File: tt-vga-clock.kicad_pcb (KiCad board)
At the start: 4 copper layers, 39 x 54 mm, 58 parts, among them J1 USB_C_Receptacle_USB2.0, J2 Conn_01x02, J3 Conn_02x04_Odd_Even, J4 Conn_01x06, J5 613012243121, J6 Conn_02x18_Odd_Even, SW1 B3U-1000P, SW2 B3U-1000P, U1 Caravel_QFN, U2 W25Q32JVSS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

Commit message: pinout for buttons, delete unneeded parts
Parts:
- removed C15: 100nF, Capacitor_SMD:C_0603_1608Metric
- removed C24, C5: 1uF, Capacitor_SMD:C_0603_1608Metric
- removed J4: Conn_01x06, Connector_PinHeader_2.54mm:PinHeader_1x06_P2.54mm_Vertical
- removed J6: Conn_02x18_Odd_Even, Connector_PinHeader_2.54mm:PinHeader_2x18_P2.54mm_Vertical
- removed R11: 5.1k, Resistor_SMD:R_0603_1608Metric
- removed R8: 10k, Resistor_SMD:R_0603_1608Metric
- removed SW2: B3U-1000P, Button_Switch_SMD:SW_SPST_B3U-1000P

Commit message: schematic done
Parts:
- removed J2: Conn_01x02, Connector_JST:JST_PH_B2B-PH-K_1x02_P2.00mm_Vertical
- added C15: 1uF, Capacitor_SMD:C_0603_1608Metric, F.Cu at (135.3, 57.4)
- added C24: 1uF, Capacitor_SMD:C_0603_1608Metric, F.Cu at (135.3, 59.9)
- added C25: 1uF, Capacitor_SMD:C_0603_1608Metric, F.Cu at (135.3, 62.4)
- added C26: 1uF, Capacitor_SMD:C_0603_1608Metric, F.Cu at (135.3, 64.9)
- added C5: 1uF, Capacitor_SMD:C_0603_1608Metric, F.Cu at (135.3, 54.9)
- added NT1: NetTie_2, NetTie:NetTie-2_SMD_Pad0.5mm, F.Cu at (113.9, 80.0)
- added NT2: NetTie_2, NetTie:NetTie-2_SMD_Pad0.5mm, F.Cu at (113.9, 81.5)
- added R11: 5.1k, Resistor_SMD:R_0603_1608Metric, F.Cu at (135.3, 69.9)
- added R16: 10k, Resistor_SMD:R_0603_1608Metric, F.Cu at (139.3, 54.9)
- added R17: 5.1k, Resistor_SMD:R_0603_1608Metric, F.Cu at (139.3, 57.4)
- added R18: 10k, Resistor_SMD:R_0603_1608Metric, F.Cu at (139.3, 59.9)
- added R19: 5.1k, Resistor_SMD:R_0603_1608Metric, F.Cu at (139.3, 62.4)
- added R20: 10k, Resistor_SMD:R_0603_1608Metric, F.Cu at (139.3, 64.9)
- added R21: 5.1k, Resistor_SMD:R_0603_1608Metric, F.Cu at (139.3, 67.4)
- added R22: 500R, Resistor_SMD:R_0603_1608Metric, F.Cu at (139.3, 69.9)
- added R23: 1k, Resistor_SMD:R_0603_1608Metric, F.Cu at (143.3, 54.9)
- added R24: 500R, Resistor_SMD:R_0603_1608Metric, F.Cu at (143.3, 57.4)
- added R25: 1k, Resistor_SMD:R_0603_1608Metric, F.Cu at (143.3, 59.9)
- added R26: 500R, Resistor_SMD:R_0603_1608Metric, F.Cu at (143.3, 62.4)
- added R27: 1k, Resistor_SMD:R_0603_1608Metric, F.Cu at (143.3, 64.9)
- added R8: 10k, Resistor_SMD:R_0603_1608Metric, F.Cu at (135.3, 67.4)
- added SW2: B3U-1000P, Button_Switch_SMD:SW_SPST_B3U-1000P, F.Cu at (148.3, 55.8)
- added SW3: B3U-1000P, Button_Switch_SMD:SW_SPST_B3U-1000P, F.Cu at (148.3, 60.1)
- added SW4: B3U-1000P, Button_Switch_SMD:SW_SPST_B3U-1000P, F.Cu at (148.3, 64.5)
- added SW5: B3U-1000P, Button_Switch_SMD:SW_SPST_B3U-1000P, F.Cu at (148.3, 68.8)
- added TP1: TestPoint, TestPoint:TestPoint_Pad_1.0x1.0mm, F.Cu at (137.3, 78.5)
- added TP2: TestPoint, TestPoint:TestPoint_Pad_1.0x1.0mm, F.Cu at (137.3, 81.5)
- J5: value 613012243121 -> DE15_Receptacle_HighDensity_MountingHoles; footprint TinyTapeout:PinSocket_2x06_P2.54mm_PMODHost1A -> Connector_Dsub:DSUB-15-HD_Female_Horizontal_P2.29x1.98mm_EdgePinOffset8.35mm_Housed_MountingHolesOffset10.89mm
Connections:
- J5 pad 1: /prj_io7 -> /red
- J5 pad 10: /prj_io14 -> GND
- J5 pad 11: GND -> unconnected-(J5-Pad11)
- J5 pad 12: +3V3 -> unconnected-(J5-Pad12)
- J5 pad 2: /prj_io8 -> /green
- J5 pad 3: /prj_io9 -> /blue
- J5 pad 4: /prj_io10 -> unconnected-(J5-Pad4)
- J5 pad 6: +3V3 -> GND
- J5 pad 7: /prj_io11 -> GND
- J5 pad 8: /prj_io12 -> GND
- J5 pad 9: /prj_io13 -> unconnected-(J5-Pad9)
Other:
- board text added: "Matt Venn"
- board text added: "TT3p5 VGA clock"
- board text removed: "(C) 2023 Pat Deegan"
- board text removed: "Caravel MVP Template"
- board text removed: "Sample Layout"
- board text removed: "This is just an example floorplan I created to get things started. Assuming you've changed the schematic, be sure to update with the appropriate Re-link/delete/replace options selected. Have fun!"
- board text removed: "v1.1"

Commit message: start layout
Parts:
- removed C11, C12, C13, C14, C17, C8: 100nF, Capacitor_SMD:C_0603_1608Metric
- removed C16: 10uF, Capacitor_SMD:C_0805_2012Metric
- removed C3: 6800pF, Capacitor_SMD:C_0603_1608Metric
- removed C4: 1uF, Capacitor_SMD:C_0603_1608Metric
- removed R2: 10k, Resistor_SMD:R_0603_1608Metric
- removed R3: 5.1k, Resistor_SMD:R_0603_1608Metric
- removed SW1: B3U-1000P, Button_Switch_SMD:SW_SPST_B3U-1000P
- added NT3: NetTie_2, NetTie:NetTie-2_SMD_Pad0.5mm, F.Cu at (104.9, 56.8)
- added TP3: TestPoint, TestPoint:TestPoint_Pad_1.0x1.0mm, F.Cu at (101.8, 49.0)
- X1: value 10MHz -> 31.5MHz
- moved SW2 60.6 mm to (95.3, 26.3), turned to 180 degrees
- moved R11 55.0 mm to (98.2, 29.3), turned to 180 degrees
- moved R8 54.5 mm to (99.5, 26.3), turned to -90 degrees
- moved FID2 50.4 mm to (127.1, 78.4)
- moved C5 48.1 mm to (94.6, 29.3)
- moved R23 41.1 mm to (103.0, 62.5), turned to -90 degrees
- moved C26 39.5 mm to (99.2, 49.0), turned to 180 degrees
- moved R25 36.0 mm to (107.4, 62.5), turned to -90 degrees
- moved R22 35.0 mm to (105.1, 62.5), turned to -90 degrees
- moved R24 34.4 mm to (109.3, 62.5), turned to -90 degrees
- moved R27 31.6 mm to (111.9, 62.5), turned to -90 degrees
- moved R26 29.6 mm to (113.8, 62.5), turned to -90 degrees
- moved SW3 28.6 mm to (125.0, 43.4)
- moved SW4 27.2 mm to (125.0, 50.4)
- moved SW5 25.9 mm to (125.0, 57.4)
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
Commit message: first pass layout
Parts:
- moved C15 14.0 mm to (125.8, 54.2)
- moved R17 14.0 mm to (122.2, 54.2)
- moved C25 14.0 mm to (126.0, 40.3)
- moved R21 14.0 mm to (122.2, 40.3)
- moved R20 14.0 mm to (121.4, 43.4)
- moved SW5 14.0 mm to (125.2, 43.4)
- moved R16 14.0 mm to (121.2, 57.4)
- moved SW3 14.0 mm to (125.0, 57.4)
- moved C7 4.49 mm to (113.8, 57.4), turned to 0 degrees
- moved C5 1.69 mm to (93.6, 30.7)
- moved R11 1.69 mm to (97.3, 30.7)
- moved R8 1.69 mm to (98.6, 27.7)
- moved SW2 1.69 mm to (94.4, 27.7)
- moved U3 0.91 mm to (123.0, 30.1)
- moved C24 0.24 mm to (126.0, 47.1)
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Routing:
- net GND: track 0.00 -> 92.2 mm, vias 0 -> 31
- net +3V3: track 0.00 -> 75.2 mm, vias 0 -> 18
- net +1V8: track 0.00 -> 52.7 mm, vias 0 -> 2
- net /prj_io7: track 0.00 -> 34.2 mm, vias 0 -> 2
- net /prj_io22: track 0.00 -> 28.7 mm, vias 0 -> 2
- net /prj_io10: track 0.00 -> 27.0 mm
- net /vsync: track 0.00 -> 26.7 mm
- net HK_SDO: track 0.00 -> 24.1 mm, vias 0 -> 2
- net /prj_io23: track 0.00 -> 23.1 mm, vias 0 -> 2
- net flash_io0: track 0.00 -> 23.1 mm
- net /prj_io9: track 0.00 -> 23.1 mm
- net flash_io1: track 0.00 -> 22.4 mm, vias 0 -> 2
- net /hsync: track 0.00 -> 22.0 mm
- net /prj_io21: track 0.00 -> 21.6 mm, vias 0 -> 2
- net HK_SDI: track 0.00 -> 20.9 mm
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- added copper zone on In1.Cu, net +3V3
- removed copper zone on B.Cu, net +3V3
- removed copper zone on F.Cu, net GND
- removed copper zone on In1.Cu, net GND

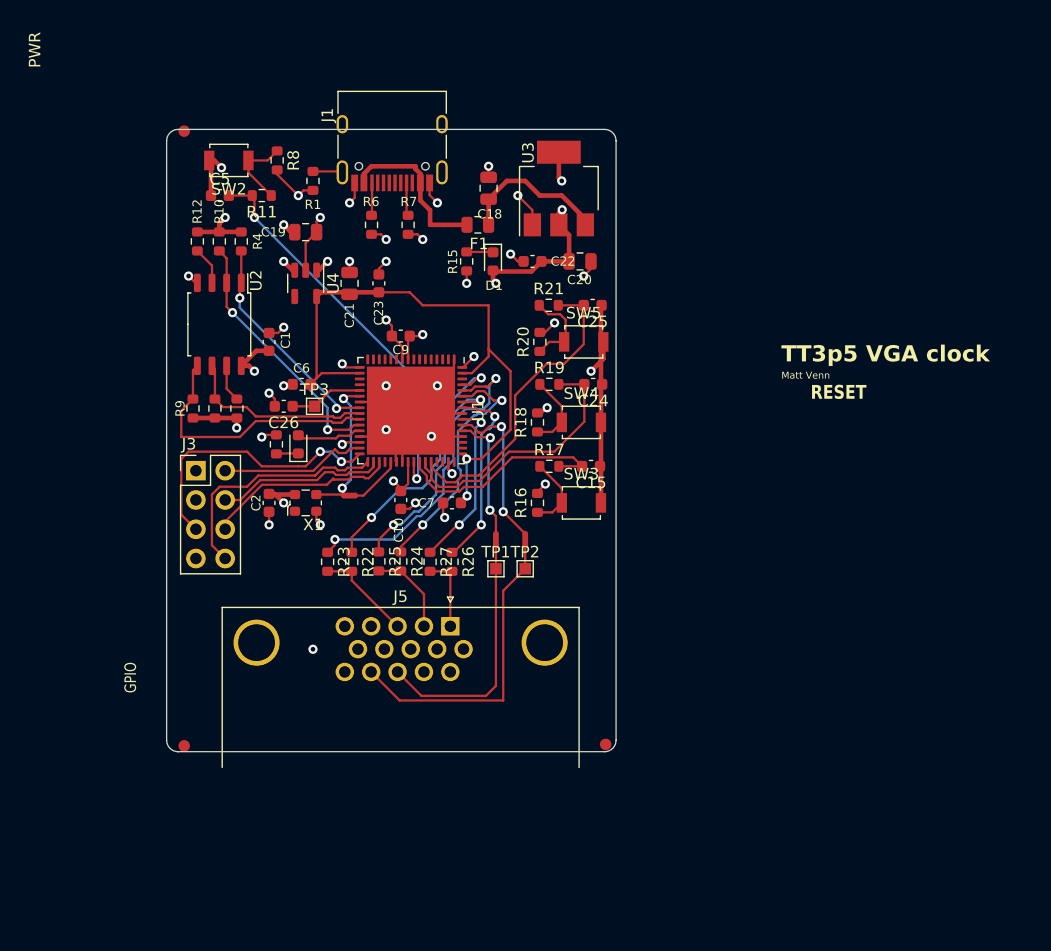
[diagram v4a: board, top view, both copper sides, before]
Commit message: oshw mark, better silk, edge cuts, all nets connected
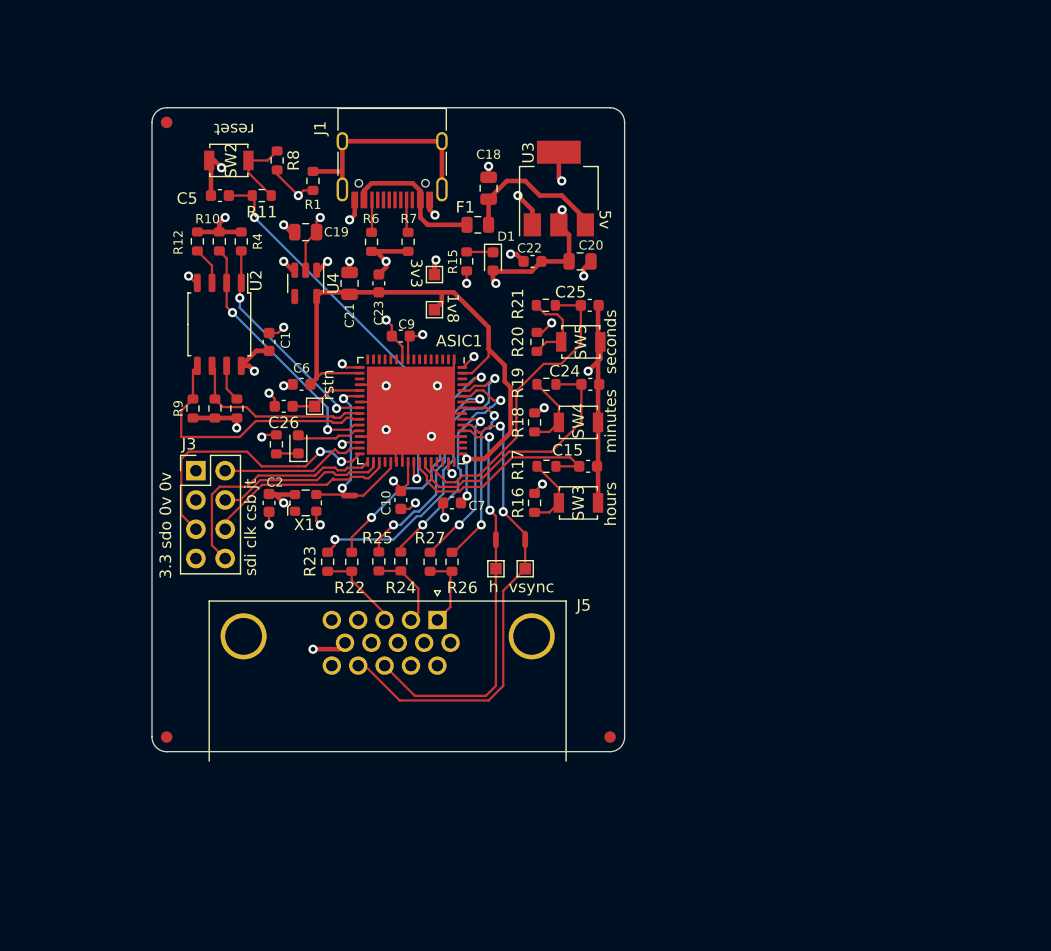
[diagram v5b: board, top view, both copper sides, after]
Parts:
- added G***: LOGO, footprints:oshw-logo, B.Cu at (108.7, 40.9)
- added TP4: TestPoint, TestPoint:TestPoint_Pad_1.0x1.0mm, F.Cu at (112.2, 37.6)
- added TP5: TestPoint, TestPoint:TestPoint_Pad_1.0x1.0mm, F.Cu at (112.2, 40.6)
- moved FID1 1.70 mm to (89.0, 24.4)
- moved FID3 1.70 mm to (89.0, 77.7)
- moved J1 1.48 mm to (108.6, 27.1)
- moved R6 1.48 mm to (106.8, 34.8)
- moved R7 1.48 mm to (110.0, 34.8)
- moved J5 1.25 mm to (112.5, 67.6)
- moved FID2 0.74 mm to (127.5, 77.7)
- moved C15 0.25 mm to (125.6, 54.2)
- moved C24 0.25 mm to (125.8, 47.1)
- moved C25 0.25 mm to (125.7, 40.3)
- moved R16 0.25 mm to (120.9, 57.4)
- moved R17 0.25 mm to (122.0, 54.2)
- moved R18 0.25 mm to (120.9, 50.4)
- moved R19 0.25 mm to (122.0, 47.1)
- moved R20 0.25 mm to (121.1, 43.4)
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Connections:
- J5 pad 0: unconnected-(J5-Pad0) -> GND
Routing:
- net Net-(J1-SHIELD): track 2.59 -> 19.6 mm
- net GND: track 92.2 -> 96.4 mm, vias 31 -> 29
- net VBUS: track 14.3 -> 12.9 mm
- net /hsync: track 22.0 -> 23.3 mm
- net +3V3: track 75.2 -> 76.5 mm, vias 18 -> 19
- net /blue: track 8.51 -> 7.50 mm
- net +1V8: track 52.7 -> 53.5 mm
- net /vsync: track 26.7 -> 27.4 mm
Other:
- board size 39 x 54 mm -> 41 x 55.9 mm
- board text added: "1v8"
- board text added: "3.3 sdo 0v 0v"
- board text added: "3v3"
- board text added: "5v"
- board text added: "ASIC1"
- board text added: "TT3p5 VGA clock Matt Venn 2023"
- board text added: "h vsync"
- board text added: "hours"
- board text added: "minutes"
- board text added: "reset"
- board text added: "rstn"
- board text added: "sdi clk csb jt"
- board text added: "seconds"
- board text removed: "GPIO"
- board text removed: "Matt Venn"
- board text removed: "PWR"
- board text removed: "RESET"
- board text removed: "TT3p5 VGA clock"

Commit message: use correct db15 fp
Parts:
- J5: footprint Connector_Dsub:DSUB-15-HD_Female_Horizontal_P2.29x1.98mm_EdgePinOffset8.35mm_Housed_MountingHolesOffset10.89mm -> footprints:db15
- moved J5 5.76 mm to (108.2, 71.4), turned to 180 degrees
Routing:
- net /blue: track 7.50 -> 8.77 mm
- net /red: track 6.65 -> 7.92 mm
- net /green: track 7.05 -> 7.80 mm
- net GND: vias 29 -> 28
